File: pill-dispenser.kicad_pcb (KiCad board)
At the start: 2 copper layers, 50 x 50 mm, 33 parts, among them Q1 AO3401A, Q2 FS8205A, U1 MT3608, U3 TP4056-42-ESOP8, U4 DW01A

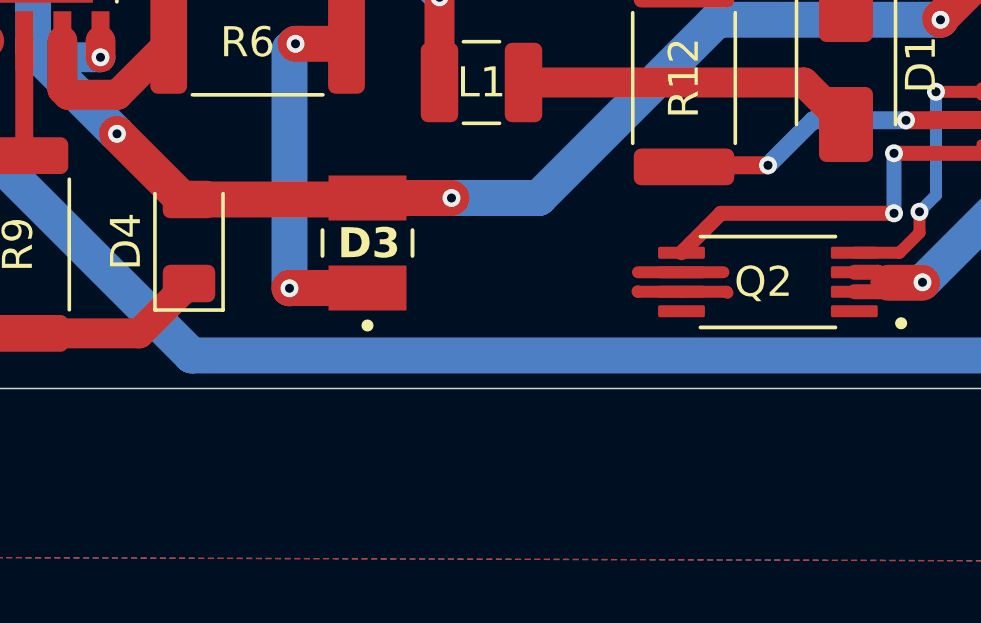
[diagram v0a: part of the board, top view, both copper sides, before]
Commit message: Updated pcb after exporting
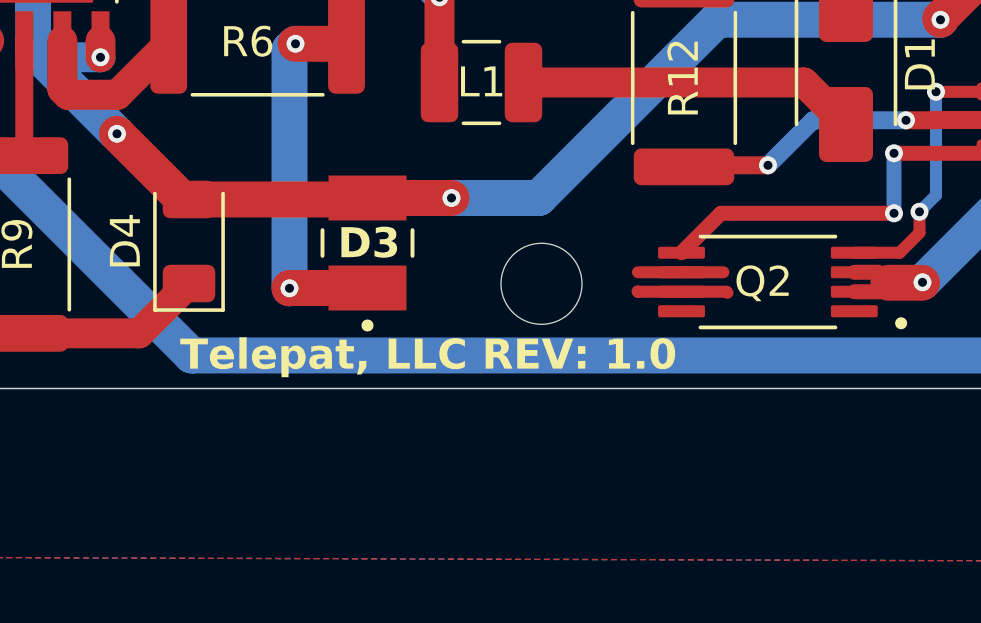
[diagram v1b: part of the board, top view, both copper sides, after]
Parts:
- added REF**: MountingHole_2.7mm_M2.5, MountingHole:MountingHole_2.7mm_M2.5, F.Cu at (124.7, 127.6)
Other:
- board text added: "Telepat, LLC REV: 1.0"
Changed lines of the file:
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@@
 			(disableapertmacros no)
 			(usegerberextensions no)
-			(usegerberattributes yes)
-			(usegerberadvancedattributes yes)
-			(creategerberjobfile yes)
+			(usegerberattributes no)
+			(usegerberadvancedattributes no)
+			(creategerberjobfile no)
 			(dashed_line_dash_ratio 12.000000)
 			(dashed_line_gap_ratio 3.000000)
@@
 			(sketchdnponfab yes)
 			(crossoutdnponfab yes)
-			(subtractmaskfromsilk no)
+			(subtractmaskfromsilk yes)
 			(outputformat 1)
 			(mirror no)
-			(drillshape 1)
+			(drillshape 0)
 			(scaleselection 1)
-			(outputdirectory "")
+			(outputdirectory "gerbers/")
 		)
 	)
@@
 		)
 	)
+	(footprint "MountingHole:MountingHole_2.7mm_M2.5"
+		(layer "F.Cu")
+		(at 124.7 127.6)
+		(descr "Mounting Hole 2.7mm, M2.5, no annular, generated by kicad-footprint-generator mountinghole.py")
+		(tags "mountinghole M2.5")
+		(property "Reference" "REF**"
+			(at 0 -3.65 0)
+			(layer "F.SilkS")
+			(hide yes)
+			(effects
+				(font
+					(size 1 1)
+					(thickness 0.15)
+				)
+			)
+		)
+		(property "Value" "MountingHole_2.7mm_M2.5"
+			(at 0 3.65 0)
+			(layer "F.Fab")
+			(effects
+				(font
+					(size 1 1)
+					(thickness 0.15)
+				)
+			)
+		)
+		(property "Datasheet" ""
+			(at 0 0 0)
+			(layer "F.Fab")
+			(hide yes)
+			(effects
+				(font
+					(size 1.27 1.27)
+					(thickness 0.15)
+				)
+			)
+		)
+		(property "Description" ""
+			(at 0 0 0)
+			(layer "F.Fab")
+			(hide yes)
+			(effects
+				(font
+					(size 1.27 1.27)
+					(thickness 0.15)
+				)
+			)
+		)
+		(attr exclude_from_pos_files exclude_from_bom)
+		(fp_circle
+			(center 0 0)
+			(end 2.7 0)
+			(stroke
+				(width 0.15)
+				(type solid)
+			)
+			(fill no)
+			(layer "Cmts.User")
+		)
+		(fp_circle
+			(center 0 0)
+			(end 2.95 0)
+			(stroke
+				(width 0.05)
+				(type solid)
+			)
+			(fill no)
+			(layer "F.CrtYd")
+		)
+		(fp_text user "${REFERENCE}"
+			(at 0 0 0)
+			(layer "F.Fab")
+			(effects
+				(font
+					(size 1 1)
+					(thickness 0.15)
+				)
+			)
+		)
+		(pad "" np_thru_hole circle
+			(at 0 0)
+			(size 2.7 2.7)
+			(drill 2.7)
+			(layers "*.Cu" "*.Mask")
+		)
+		(embedded_fonts no)
+	)
 	(footprint "Capacitor_SMD:C_1210_3225Metric"
 		(layer "F.Cu")
@@
 		(layer "Edge.Cuts")
 	)
+	(gr_text "Telepat, LLC REV: 1.0"
+		(at 112.65 130.55 0)
+		(layer "F.SilkS")
+		(effects
+			(font
+				(size 1 1)
+				(thickness 0.2)
+				(bold yes)
+			)
+			(justify left bottom)
+		)
+	)
 	(segment
